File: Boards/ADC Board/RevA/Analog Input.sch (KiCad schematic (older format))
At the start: 1 part

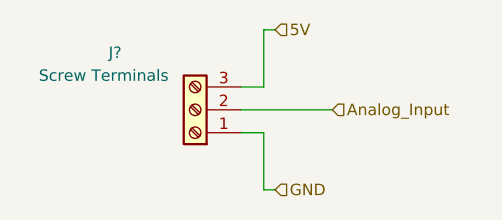
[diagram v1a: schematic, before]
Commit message: Connected power regulator to ADC and micro boards. Added no connects to headers on ADC board. Preformed some footprinting operations on ADC board.
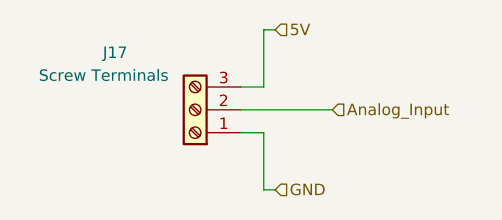
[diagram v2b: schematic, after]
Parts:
- gave numbers to parts that had none: 1
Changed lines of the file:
@@
 AR Path="/616423D2/61653B35" Ref="J?"  Part="1"
 AR Path="/616425FE/61653B35" Ref="J?"  Part="1"
-AR Path="/6164D83E/61653B35" Ref="J?"  Part="1"
-AR Path="/616568DC/61653B35" Ref="J?"  Part="1"
-AR Path="/61657053/61653B35" Ref="J?"  Part="1"
-AR Path="/616571E9/61653B35" Ref="J?"  Part="1"
-F 0 "J?" H 2000 1050 50  0000 C CNN
+AR Path="/6164D83E/61653B35" Ref="J14"  Part="1"
+AR Path="/616568DC/61653B35" Ref="J15"  Part="1"
+AR Path="/61657053/61653B35" Ref="J16"  Part="1"
+AR Path="/616571E9/61653B35" Ref="J17"  Part="1"
+F 0 "J17" H 2000 1050 50  0000 C CNN
 F 1 "Screw Terminals" H 2050 1150 50  0000 C CNN
 F 2 "" H 1650 1300 50  0001 C CNN

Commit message: Fixed regulator nonsense on ADC board. Rules checked both ADC and micro boards. Fixed interconnect on ADC board.
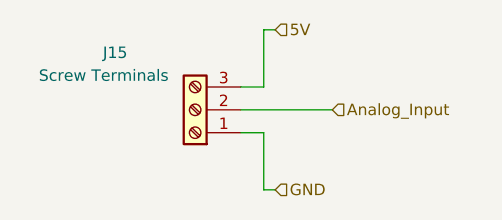
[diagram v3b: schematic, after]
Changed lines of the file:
@@
 $Descr A4 11693 8268
 encoding utf-8
-Sheet 7 11
+Sheet 8 11
 Title ""
 Date ""
@@
 AR Path="/61657053/61653B35" Ref="J16"  Part="1"
 AR Path="/616571E9/61653B35" Ref="J17"  Part="1"
-F 0 "J17" H 2000 1050 50  0000 C CNN
+F 0 "J15" H 2000 1050 50  0000 C CNN
 F 1 "Screw Terminals" H 2050 1150 50  0000 C CNN
 F 2 "" H 1650 1300 50  0001 C CNN

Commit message: Began PCB layout for ADC board. Fixed annotations for ADC and micro boards.
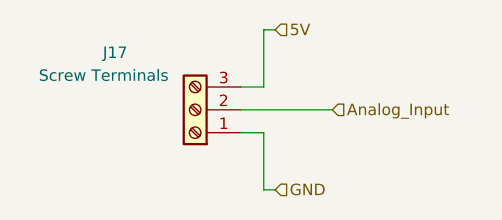
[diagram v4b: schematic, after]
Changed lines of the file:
@@
 $Descr A4 11693 8268
 encoding utf-8
-Sheet 8 11
+Sheet 10 11
 Title ""
 Date ""
@@
 AR Path="/61657053/61653B35" Ref="J16"  Part="1"
 AR Path="/616571E9/61653B35" Ref="J17"  Part="1"
-F 0 "J15" H 2000 1050 50  0000 C CNN
+F 0 "J17" H 2000 1050 50  0000 C CNN
 F 1 "Screw Terminals" H 2050 1150 50  0000 C CNN
 F 2 "" H 1650 1300 50  0001 C CNN

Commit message: Completed footprint associations for ADC board. Generated netlist for ADC board. Started PCB design for ADC board.
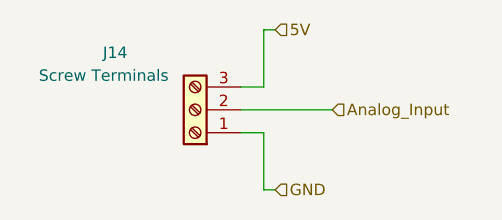
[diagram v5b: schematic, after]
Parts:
- J14: footprint (none) -> Connector_PinHeader_2.54mm:PinHeader_1x03_P2.54mm_Vertical
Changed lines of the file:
@@
 $Descr A4 11693 8268
 encoding utf-8
-Sheet 10 11
+Sheet 7 11
 Title ""
 Date ""
@@
 AR Path="/61657053/61653B35" Ref="J16"  Part="1"
 AR Path="/616571E9/61653B35" Ref="J17"  Part="1"
-F 0 "J17" H 2000 1050 50  0000 C CNN
+F 0 "J14" H 2000 1050 50  0000 C CNN
 F 1 "Screw Terminals" H 2050 1150 50  0000 C CNN
-F 2 "" H 1650 1300 50  0001 C CNN
+F 2 "Connector_PinHeader_2.54mm:PinHeader_1x03_P2.54mm_Vertical" H 1650 1300 50  0001 C CNN
 F 3 "~" H 1650 1300 50  0001 C CNN
 	1    1650 1300
